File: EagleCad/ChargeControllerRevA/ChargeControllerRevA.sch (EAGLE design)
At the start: 59 parts, among them Q1 SI7135DP, Q2 SI7135DP

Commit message: renamed RC
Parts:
- removed CC1, CC2, CVCC: (no value), rcl:C-US025-050X050
- removed R2, RC, RS1: (no value), rcl:R-US_0309/12
- removed VOUT(1): (no value), wirepad:3,81/1,4
- added C1, C4, C7: (no value), rcl:C-US025-050X050
- added R2', R21, R7: (no value), rcl:R-US_0309/12
- renumbered CF to C3, CIN1 to C10, CIN3 to C14, CIN4 to C13, CIN5 to C11, CIN6 to C12, COUT to C9, CSS to C6, RS2 to R14
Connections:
- net BATT: now also R18.1; no longer R20.1
- net GND: now also C2.2, C5.2, C8.2, R12.1, R20.1, R21.1, R3.2, R5.1, R7.2; no longer CC1.2, CC2.2, CVCC.2, R1.1, R11.1, R17.1, R18.1, R4.2, R5.2
- net N$10: now also R3.1; no longer R4.1
- net N$11: now also C4.1; no longer C5.1
- net N$12: now also R2'.1; no longer R8.1
- net N$13: now also C2.1; no longer CVCC.1
- net N$16: now also R8.2; no longer R6.2
- net N$19: now also R9.1; no longer R12.1
- net N$2: now also C7.1, R7.1; no longer C2.1, R5.1
- net N$20: now also C1.1; no longer C8.1
- net N$21: now also R15.2; no longer R3.2
- net N$28: now also R10.1, R11.2; no longer R15.1, R16.2
- net N$29: now also R11.1, R12.2; no longer R16.1, R17.2
- net N$3: now also C7.2, R8.1; no longer C2.2, R6.1
- net N$35: now also R20.2; no longer R11.2
- net N$36: now also R21.2; no longer R18.2
- net N$4: now also C5.1, R6.2, R9.2; no longer CC2.1, R12.2, RC.2
- net N$40: now also R16.1, R17.2; no longer R10.2, R9.1
- net N$41: now also R17.1, R18.2; no longer R10.1, R20.2
- net N$42: now also R15.1, R16.2; no longer R3.1, R9.2
- net N$5: now also C8.1, R6.1; no longer CC1.1, RC.1
- net N$7: now also R4.1, R5.2; no longer R1.2, R2.1
- net SW1: now also C4.2; no longer C5.2
- net SW2: now also C1.2; no longer C8.2
- net VIN: now also CIN2.1, R1.2, R2'.2; no longer CIN.1, R8.2, RS1.2
- net VIN+: now also CIN.1, R1.1, R10.2; no longer CIN2.1, R15.2, RS1.1
- net VOUT(1): now also R4.2; no longer R2.2, VOUT(1).P
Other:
- moved on the sheet: C2, C5, C8, CIN, CIN2, R1, R10, R11, R12, R15, R16, R17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

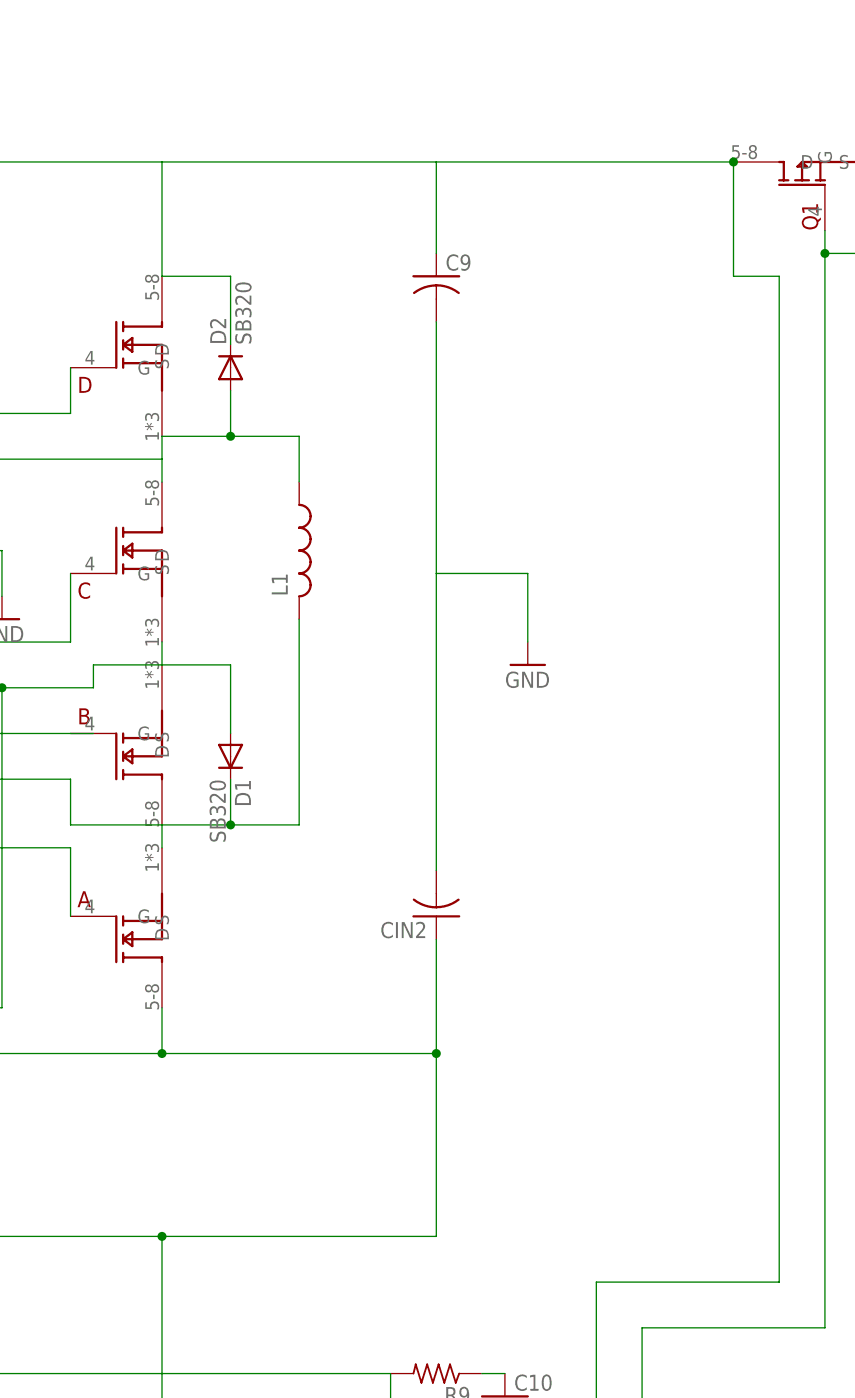
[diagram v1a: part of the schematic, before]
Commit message: in/out caps added
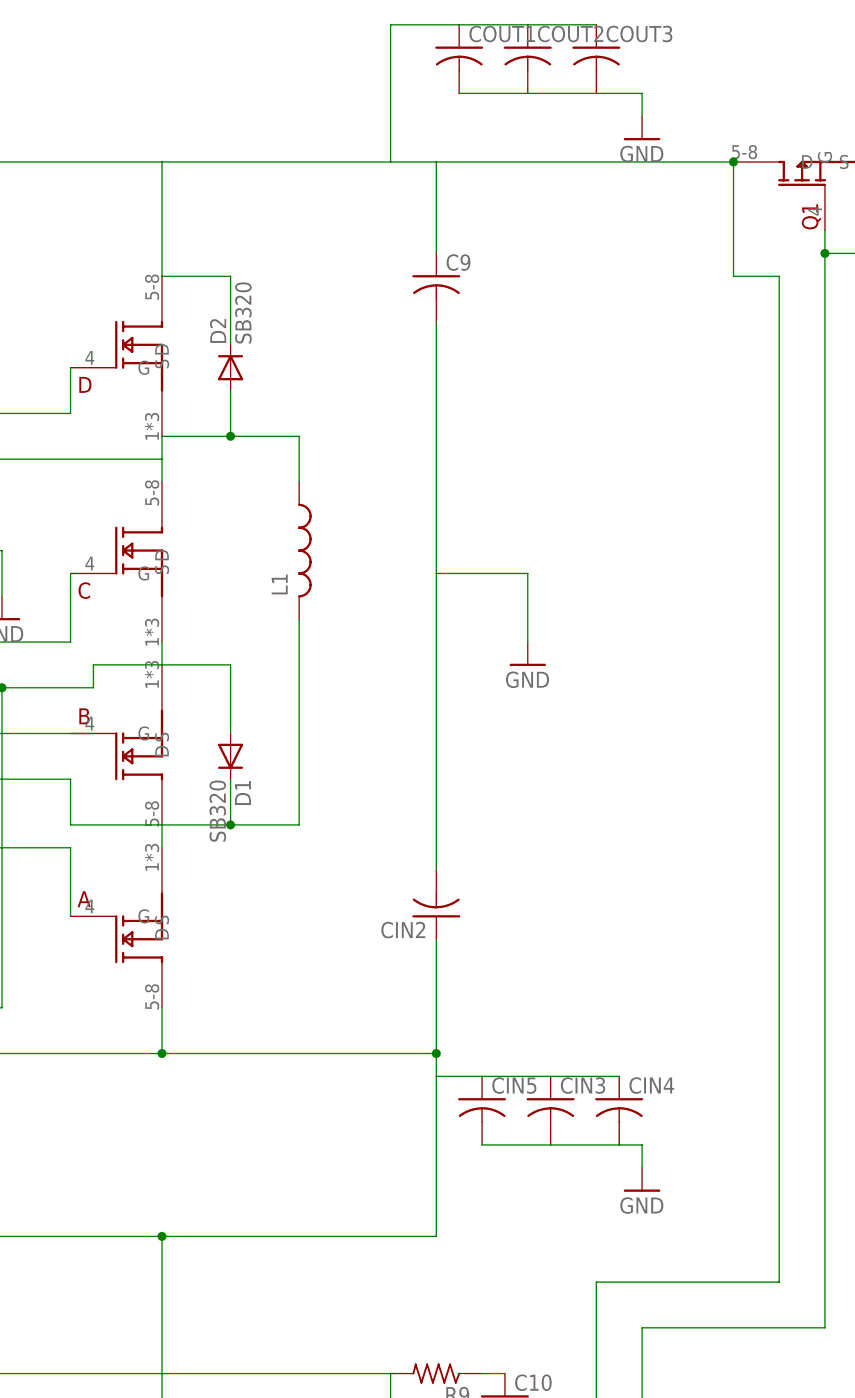
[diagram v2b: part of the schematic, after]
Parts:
- added CIN3, CIN4, CIN5, COUT1, COUT2, COUT3: (no value), rcl:C-US025-050X050
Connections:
- net GND: now also CIN3.2, CIN4.2, CIN5.2, COUT1.2, COUT2.2, COUT3.2
- net VIN: now also CIN3.1, CIN4.1, CIN5.1
- net VOUT(1): now also COUT1.1, COUT2.1, COUT3.1
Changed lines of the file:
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@@
 <part name="-FLT" library="wirepad" deviceset="3,81/1,4" device=""/>
 <part name="U$2" library="SeniorDesign" deviceset="LTC4000-1(B)" device="GN" value="LTC4000-1"/>
+<part name="CIN5" library="rcl" deviceset="C-US" device="025-050X050"/>
+<part name="CIN3" library="rcl" deviceset="C-US" device="025-050X050"/>
+<part name="CIN4" library="rcl" deviceset="C-US" device="025-050X050"/>
+<part name="GND9" library="supply1" deviceset="GND" device=""/>
+<part name="COUT1" library="rcl" deviceset="C-US" device="025-050X050"/>
+<part name="COUT2" library="rcl" deviceset="C-US" device="025-050X050"/>
+<part name="COUT3" library="rcl" deviceset="C-US" device="025-050X050"/>
+<part name="GND10" library="supply1" deviceset="GND" device=""/>
 </parts>
 <sheets>
@@
 <instance part="-FLT" gate="1" x="167.64" y="-81.28"/>
 <instance part="U$2" gate="G$1" x="210.82" y="-63.5"/>
+<instance part="CIN5" gate="G$1" x="200.66" y="7.62"/>
+<instance part="CIN3" gate="G$1" x="208.28" y="7.62"/>
+<instance part="CIN4" gate="G$1" x="215.9" y="7.62"/>
+<instance part="GND9" gate="1" x="218.44" y="-2.54"/>
+<instance part="COUT1" gate="G$1" x="198.12" y="124.46"/>
+<instance part="COUT2" gate="G$1" x="205.74" y="124.46"/>
+<instance part="COUT3" gate="G$1" x="213.36" y="124.46"/>
+<instance part="GND10" gate="1" x="218.44" y="114.3"/>
 </instances>
 <busses>
@@
 <wire x1="38.1" y1="58.42" x2="38.1" y2="111.76" width="0.1524" layer="91"/>
 <wire x1="38.1" y1="111.76" x2="165.1" y2="111.76" width="0.1524" layer="91"/>
-<wire x1="165.1" y1="111.76" x2="195.58" y2="111.76" width="0.1524" layer="91"/>
+<wire x1="165.1" y1="111.76" x2="190.5" y2="111.76" width="0.1524" layer="91"/>
 <pinref part="D2" gate="1" pin="C"/>
+<wire x1="190.5" y1="111.76" x2="195.58" y2="111.76" width="0.1524" layer="91"/>
 <wire x1="172.72" y1="91.44" x2="172.72" y2="99.06" width="0.1524" layer="91"/>
 <pinref part="D" gate="G$1" pin="D"/>
@@
 <junction x="228.6" y="111.76"/>
 <pinref part="U$2" gate="G$1" pin="IID"/>
+<pinref part="COUT3" gate="G$1" pin="1"/>
+<pinref part="COUT2" gate="G$1" pin="1"/>
+<wire x1="213.36" y1="127" x2="205.74" y2="127" width="0.1524" layer="91"/>
+<pinref part="COUT1" gate="G$1" pin="1"/>
+<wire x1="205.74" y1="127" x2="198.12" y2="127" width="0.1524" layer="91"/>
+<wire x1="198.12" y1="127" x2="190.5" y2="127" width="0.1524" layer="91"/>
+<wire x1="190.5" y1="127" x2="190.5" y2="111.76" width="0.1524" layer="91"/>
 </segment>
 </net>
@@
 <wire x1="134.62" y1="-7.62" x2="165.1" y2="-7.62" width="0.1524" layer="91"/>
 <wire x1="165.1" y1="-7.62" x2="195.58" y2="-7.62" width="0.1524" layer="91"/>
-<wire x1="195.58" y1="-7.62" x2="195.58" y2="12.7" width="0.1524" layer="91"/>
+<wire x1="195.58" y1="-7.62" x2="195.58" y2="10.16" width="0.1524" layer="91"/>
 <junction x="195.58" y="12.7"/>
+<wire x1="195.58" y1="10.16" x2="195.58" y2="12.7" width="0.1524" layer="91"/>
 <wire x1="177.8" y1="-53.34" x2="165.1" y2="-53.34" width="0.1524" layer="91"/>
 <wire x1="165.1" y1="-53.34" x2="165.1" y2="-7.62" width="0.1524" layer="91"/>
 <junction x="165.1" y="-7.62"/>
 <pinref part="U$2" gate="G$1" pin="CLN"/>
+<pinref part="CIN4" gate="G$1" pin="1"/>
+<pinref part="CIN3" gate="G$1" pin="1"/>
+<wire x1="215.9" y1="10.16" x2="208.28" y2="10.16" width="0.1524" layer="91"/>
+<pinref part="CIN5" gate="G$1" pin="1"/>
+<wire x1="208.28" y1="10.16" x2="200.66" y2="10.16" width="0.1524" layer="91"/>
+<wire x1="200.66" y1="10.16" x2="195.58" y2="10.16" width="0.1524" layer="91"/>
 </segment>
 </net>
@@
 <pinref part="U$2" gate="G$1" pin="GND'"/>
 </segment>
-</net>
+<segment>
+<pinref part="CIN5" gate="G$1" pin="2"/>
+<pinref part="CIN3" gate="G$1" pin="2"/>
+<wire x1="200.66" y1="2.54" x2="208.28" y2="2.54" width="0.1524" layer="91"/>
+<pinref part="CIN4" gate="G$1" pin="2"/>
+<wire x1="208.28" y1="2.54" x2="215.9" y2="2.54" width="0.1524" layer="91"/>
+<wire x1="215.9" y1="2.54" x2="218.44" y2="2.54" width="0.1524" layer="91"/>
+<wire x1="218.44" y1="2.54" x2="218.44" y2="0" width="0.1524" layer="91"/>
+<pinref part="GND9" gate="1" pin="GND"/>
+</segment>
+<segment>
+<pinref part="COUT1" gate="G$1" pin="2"/>
+<pinref part="COUT2" gate="G$1" pin="2"/>
+<wire x1="198.12" y1="119.38" x2="205.74" y2="119.38" width="0.1524" layer="91"/>
+<pinref part="COUT3" gate="G$1" pin="2"/>
+<wire x1="205.74" y1="119.38" x2="213.36" y2="119.38" width="0.1524" layer="91"/>
+<wire x1="213.36" y1="119.38" x2="218.44" y2="119.38" width="0.1524" layer="91"/>
+<wire x1="218.44" y1="119.38" x2="218.44" y2="116.84" width="0.1524" layer="91"/>
+<pinref part="GND10" gate="1" pin="GND"/>
+</segment>
+</net>
